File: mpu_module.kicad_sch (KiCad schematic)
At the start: 11 parts

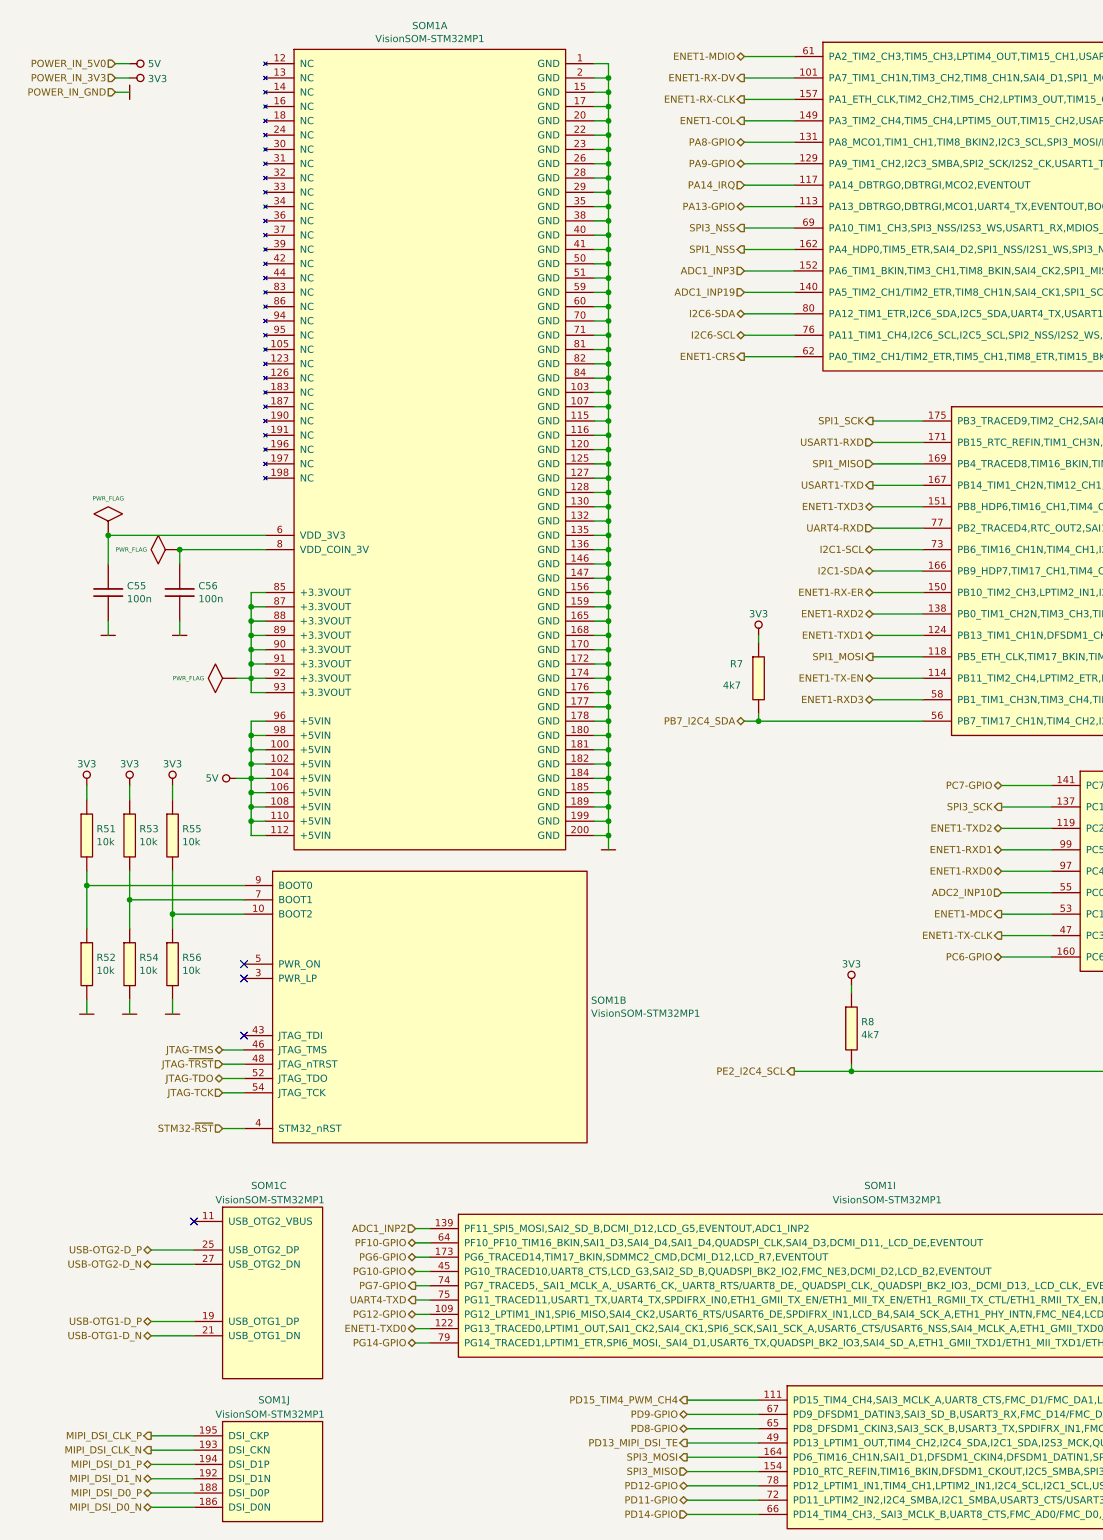
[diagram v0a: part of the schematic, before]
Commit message: Corrected schematic
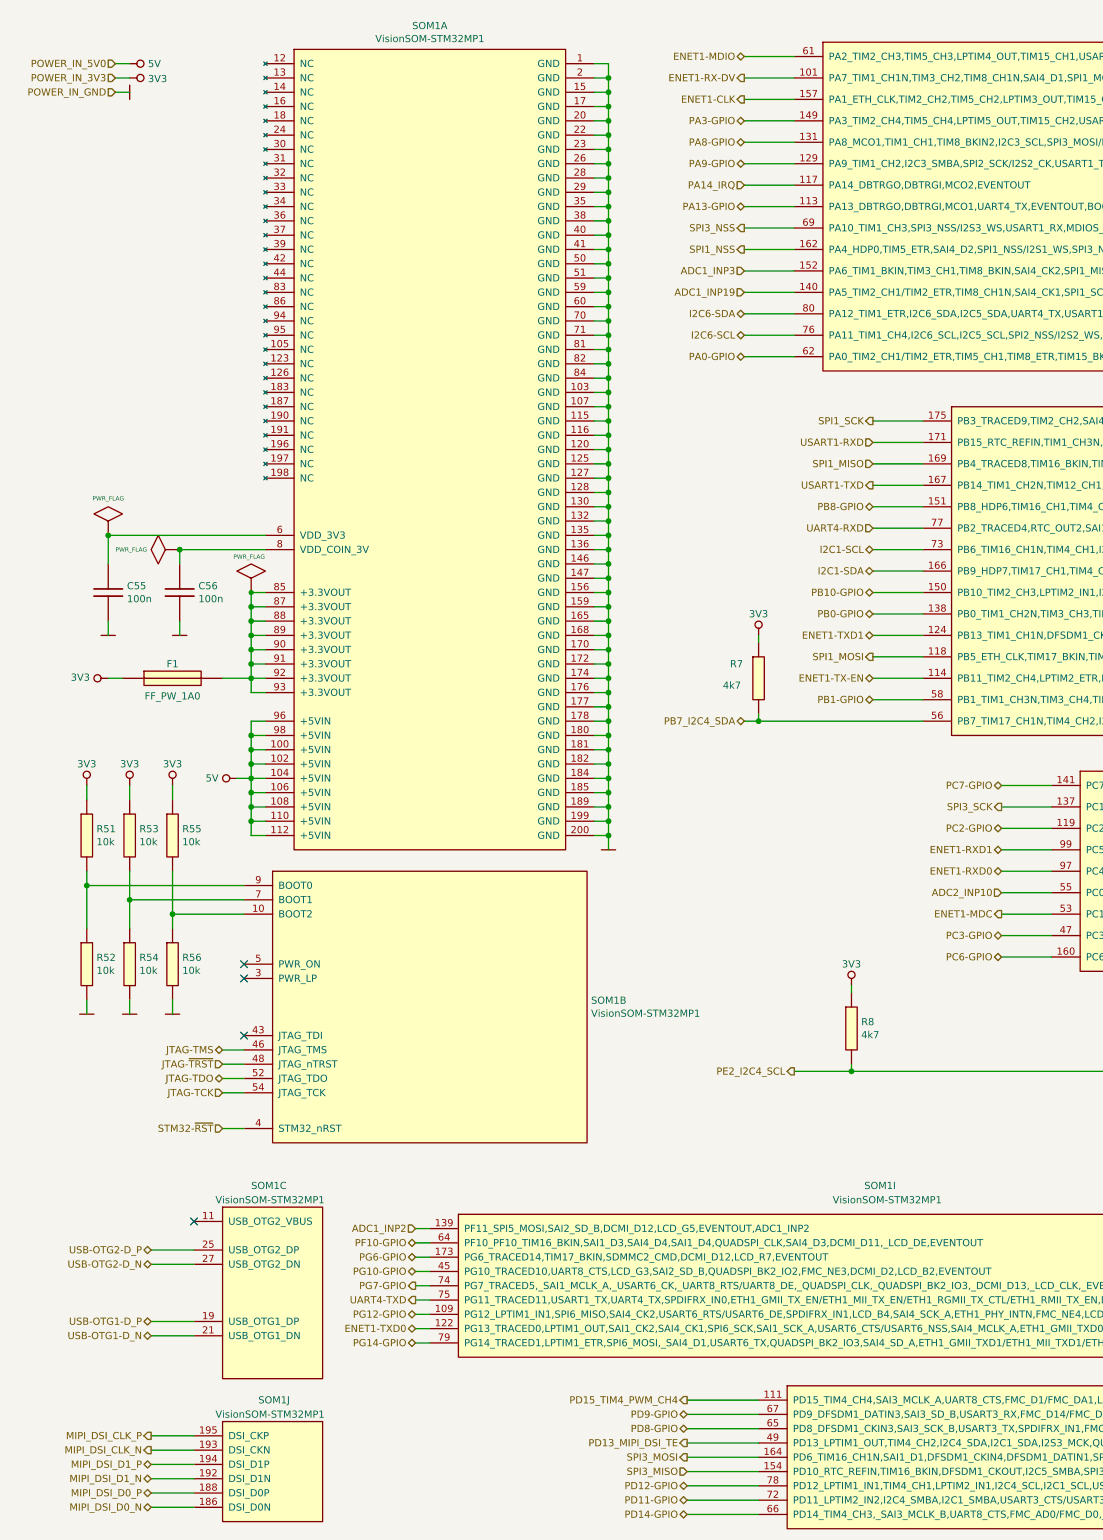
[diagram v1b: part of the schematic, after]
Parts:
- added F1: FF_PW_1A0, Smd_Fuses:Fuse_0603-FF_PW_1A0, symbol Smd_Fuses:FF_PW_1A0
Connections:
- net 3V3: now also F1.1
- net at SOM1.85 (+3.3VOUT), SOM1.87 (+3.3VOUT), SOM1.88 (+3.3VOUT)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: now also F1.2
- net ENET1-COL renamed PA3-GPIO
- net ENET1-CRS renamed PA0-GPIO
- net ENET1-RX-CLK renamed ENET1-CLK
- net ENET1-RX-ER renamed PB10-GPIO
- net ENET1-RXD2 renamed PB0-GPIO
- net ENET1-RXD3 renamed PB1-GPIO
- net ENET1-TX-CLK renamed PC3-GPIO
- net ENET1-TXD2 renamed PC2-GPIO
- net ENET1-TXD3 renamed PB8-GPIO
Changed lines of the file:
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@@
   (junction (at 118.11 158.75) (diameter 1.016) (color 0 0 0 0)
   )
+  (junction (at 54.61 115.57) (diameter 0) (color 0 0 0 0)
+  )
   (junction (at 118.11 135.89) (diameter 1.016) (color 0 0 0 0)
   )
@@
     (stroke (width 0) (type solid) (color 0 0 0 0))
   )
-  (wire (pts (xy 54.61 130.81) (xy 52.07 130.81))
-    (stroke (width 0) (type solid) (color 0 0 0 0))
-  )
   (wire (pts (xy 118.11 80.01) (xy 118.11 82.55))
     (stroke (width 0) (type solid) (color 0 0 0 0))
@@
     (stroke (width 0) (type solid) (color 0 0 0 0))
   )
+  (wire (pts (xy 29.21 130.81) (xy 31.75 130.81))
+    (stroke (width 0) (type default) (color 0 0 0 0))
+  )
   (wire (pts (xy 86.36 248.92) (xy 83.82 248.92))
     (stroke (width 0) (type solid) (color 0 0 0 0))
@@
     (stroke (width 0) (type solid) (color 0 0 0 0))
   )
+  (wire (pts (xy 49.53 130.81) (xy 54.61 130.81))
+    (stroke (width 0) (type default) (color 0 0 0 0))
+  )
   (wire (pts (xy 173.99 111.76) (xy 165.1 111.76))
     (stroke (width 0) (type solid) (color 0 0 0 0))
@@
     )
   )
-  (hierarchical_label "ENET1-COL" (shape output) (at 142.24 31.75 180)
-    (effects (font (size 1.27 1.27)) (justify right))
-  )
   (hierarchical_label "SPI3_MOSI" (shape output) (at 132.08 269.24 180)
     (effects (font (size 1.27 1.27)) (justify right))
@@
     (effects (font (size 1.27 1.27)) (justify right))
   )
-  (hierarchical_label "ENET1-TXD2" (shape bidirectional) (at 187.96 157.48 180)
-    (effects (font (size 1.27 1.27)) (justify right))
-  )
   (hierarchical_label "PG6-GPIO" (shape bidirectional) (at 83.82 233.68 180)
     (effects (font (size 1.27 1.27)) (justify right))
@@
     (effects (font (size 1.27 1.27)) (justify right))
   )
+  (hierarchical_label "PC3-GPIO" (shape bidirectional) (at 187.96 176.53 180)
+    (effects (font (size 1.27 1.27)) (justify right))
+  )
   (hierarchical_label "UART4-TXD" (shape output) (at 83.82 241.3 180)
     (effects (font (size 1.27 1.27)) (justify right))
   )
-  (hierarchical_label "USB-OTG1-D_P" (shape bidirectional) (at 36.83 245.11 180)
+  (hierarchical_label "PA3-GPIO" (shape bidirectional) (at 142.24 31.75 180)
     (effects (font (size 1.27 1.27)) (justify right))
   )
-  (hierarchical_label "SPI3_MISO" (shape input) (at 132.08 271.78 180)
+  (hierarchical_label "USB-OTG1-D_P" (shape bidirectional) (at 36.83 245.11 180)
     (effects (font (size 1.27 1.27)) (justify right))
   )
-  (hierarchical_label "ENET1-RXD2" (shape bidirectional) (at 165.1 119.38 180)
+  (hierarchical_label "SPI3_MISO" (shape input) (at 132.08 271.78 180)
     (effects (font (size 1.27 1.27)) (justify right))
   )
@@
     (effects (font (size 1.27 1.27)) (justify right))
   )
-  (hierarchical_label "ENET1-RXD3" (shape bidirectional) (at 165.1 134.62 180)
+  (hierarchical_label "PA0-GPIO" (shape bidirectional) (at 142.24 73.66 180)
+    (effects (font (size 1.27 1.27)) (justify right))
+  )
+  (hierarchical_label "PB0-GPIO" (shape bidirectional) (at 165.1 119.38 180)
     (effects (font (size 1.27 1.27)) (justify right))
   )
@@
     (effects (font (size 1.27 1.27)) (justify right))
   )
-  (hierarchical_label "ENET1-CRS" (shape output) (at 142.24 73.66 180)
-    (effects (font (size 1.27 1.27)) (justify right))
-  )
   (hierarchical_label "ENET1-TXD1" (shape bidirectional) (at 165.1 123.19 180)
     (effects (font (size 1.27 1.27)) (justify right))
@@
     (effects (font (size 1.27 1.27)) (justify right))
   )
+  (hierarchical_label "PC2-GPIO" (shape bidirectional) (at 187.96 157.48 180)
+    (effects (font (size 1.27 1.27)) (justify right))
+  )
   (hierarchical_label "PD8-GPIO" (shape bidirectional) (at 132.08 264.16 180)
     (effects (font (size 1.27 1.27)) (justify right))
@@
     (effects (font (size 1.27 1.27)) (justify right))
   )
-  (hierarchical_label "ENET1-TXD3" (shape bidirectional) (at 165.1 100.33 180)
-    (effects (font (size 1.27 1.27)) (justify right))
-  )
-  (hierarchical_label "ENET1-TX-CLK" (shape output) (at 187.96 176.53 180)
+  (hierarchical_label "PB1-GPIO" (shape bidirectional) (at 165.1 134.62 180)
     (effects (font (size 1.27 1.27)) (justify right))
   )
@@
     (effects (font (size 1.27 1.27)) (justify right))
   )
-  (hierarchical_label "ENET1-RX-ER" (shape bidirectional) (at 165.1 115.57 180)
+  (hierarchical_label "PB8-GPIO" (shape bidirectional) (at 165.1 100.33 180)
     (effects (font (size 1.27 1.27)) (justify right))
   )
-  (hierarchical_label "ENET1-RX-CLK" (shape output) (at 142.24 27.94 180)
+  (hierarchical_label "ENET1-CLK" (shape output) (at 142.24 27.94 180)
     (effects (font (size 1.27 1.27)) (justify right))
   )
@@
     (effects (font (size 1.27 1.27)) (justify right))
   )
-  (hierarchical_label "PD14-GPIO" (shape input) (at 132.08 279.4 180)
+  (hierarchical_label "PD14-GPIO" (shape bidirectional) (at 132.08 279.4 180)
     (effects (font (size 1.27 1.27)) (justify right))
   )
@@
     (effects (font (size 1.27 1.27)) (justify right))
   )
+  (hierarchical_label "PB10-GPIO" (shape bidirectional) (at 165.1 115.57 180)
+    (effects (font (size 1.27 1.27)) (justify right))
+  )
   (hierarchical_label "PB7_I2C4_SDA" (shape bidirectional) (at 142.24 138.43 180)
     (effects (font (size 1.27 1.27)) (justify right))
@@
     (pin "1")
   )
-  (symbol (lib_id "power:PWR_FLAG") (at 52.07 130.81 90) (unit 1)
+  (symbol (lib_id "power:PWR_FLAG") (at 54.61 115.57 0) (unit 1)
     (in_bom yes) (on_board yes)
-    (property "Reference" "#FLG0107" (id 0) (at 45.212 130.81 0)
+    (property "Reference" "#FLG0107" (id 0) (at 54.61 108.712 0)
       (effects (font (size 0.762 0.762)) hide)
     )
-    (property "Value" "PWR_FLAG" (id 1) (at 46.2788 130.81 90)
+    (property "Value" "PWR_FLAG" (id 1) (at 51.435 109.22 0)
       (effects (font (size 0.762 0.762)) (justify left))
     )
-    (property "Footprint" "" (id 2) (at 52.07 130.81 0)
+    (property "Footprint" "" (id 2) (at 54.61 115.57 0)
       (effects (font (size 1.524 1.524)))
     )
-    (property "Datasheet" "" (id 3) (at 52.07 130.81 0)
+    (property "Datasheet" "" (id 3) (at 54.61 115.57 0)
       (effects (font (size 1.524 1.524)))
     )
@@
     (pin "1")
   )
+  (symbol (lib_id "power:3V3_NO_GLOBAL") (at 29.21 130.81 90) (unit 1)
+    (in_bom yes) (on_board yes)
+    (property "Reference" "#PWR76" (id 0) (at 26.67 130.81 0)
+      (effects (font (size 1.016 1.016)) hide)
+    )
+    (property "Value" "3V3" (id 1) (at 25.9588 130.6576 90)
+      (effects (font (size 1.27 1.27)) (justify left))
+    )
+    (property "Footprint" "" (id 2) (at 29.21 130.81 0)
+      (effects (font (size 1.524 1.524)))
+    )
+    (property "Datasheet" "" (id 3) (at 29.21 130.81 0)
+      (effects (font (size 1.524 1.524)))
+    )
+    (pin "1")
+  )
+  (symbol (lib_id "Smd_Fuses:FF_PW_1A0") (at 40.64 130.81 0) (unit 1)
+    (in_bom yes) (on_board yes)
+    (property "Reference" "F1" (id 0) (at 40.64 128.27 0))
+    (property "Value" "FF_PW_1A0" (id 1) (at 40.64 133.985 0))
+    (property "Footprint" "Smd_Fuses:Fuse_0603-FF_PW_1A0" (id 2) (at 40.64 142.24 0)
+      (effects (font (size 1.27 1.27)) hide)
+    )
+    (property "Datasheet" "https://www.tme.eu/Document/d23fed0116a9e0192c3db408cb2a3cd4/81.pdf" (id 3) (at 40.64 142.24 0)
+      (effects (font (size 1.27 1.27)) hide)
+    )
+    (property "Manufacturer" "ESKA" (id 4) (at 40.64 130.81 0)
+      (effects (font (size 1.27 1.27)) hide)
+    )
+    (property "Manufacturer Part Number" "FUSE 0603-FF PW 1A" (id 5) (at 40.64 130.81 0)
+      (effects (font (size 1.27 1.27)) hide)
+    )
+    (property "Supplier" "Tme" (id 6) (at 40.64 130.81 0)
+      (effects (font (size 1.27 1.27)) hide)
+    )
+    (property "Supplier Part Number" "BSMD0603-SS1.0" (id 7) (at 40.64 130.81 0)
+      (effects (font (size 1.27 1.27)) hide)
+    )
+    (property "URL" "https://www.tme.eu/pl/details/bsmd0603-ss1.0/bezpieczniki-smd-0603-superszybkie/eska/fuse-0603-ff-pw-1a0/" (id 8) (at 40.64 130.81 0)
+      (effects (font (size 1.27 1.27)) hide)
+    )
+    (property "Price@1pc" "0,95" (id 9) (at 40.64 130.81 0)
+      (effects (font (size 1.27 1.27)) hide)
+    )
+    (property "Price@1000pcs" "0,55" (id 10) (at 40.64 130.81 0)
+      (effects (font (size 1.27 1.27)) hide)
+    )
+    (property "Developer" "MW" (id 11) (at 40.64 130.81 0)
+      (effects (font (size 1.27 1.27)) hide)
+    )
+    (property "Package" "0603" (id 12) (at 40.64 130.81 0)
+      (effects (font (size 1.27 1.27)) hide)
+    )
+    (property "LCSC Part #(optional)" "" (id 13) (at 40.64 130.81 0)
+      (effects (font (size 1.27 1.27)) hide)
+    )
+    (pin "1")
+    (pin "2")
+  )
 )

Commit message: Rebuild board
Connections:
- net ENET1-RX-DV renamed ENET1-CRS-DV
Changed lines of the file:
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@@
     (effects (font (size 1.27 1.27)) (justify right))
   )
-  (hierarchical_label "ENET1-RX-DV" (shape output) (at 142.24 24.13 180)
+  (hierarchical_label "ENET1-CRS-DV" (shape output) (at 142.24 24.13 180)
     (effects (font (size 1.27 1.27)) (justify right))
   )

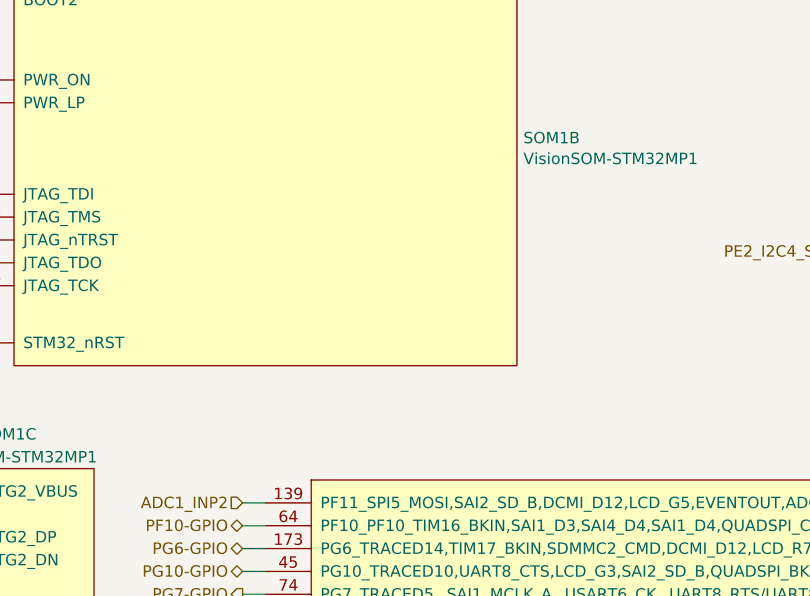
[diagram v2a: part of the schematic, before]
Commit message: Cleared all errors DRC
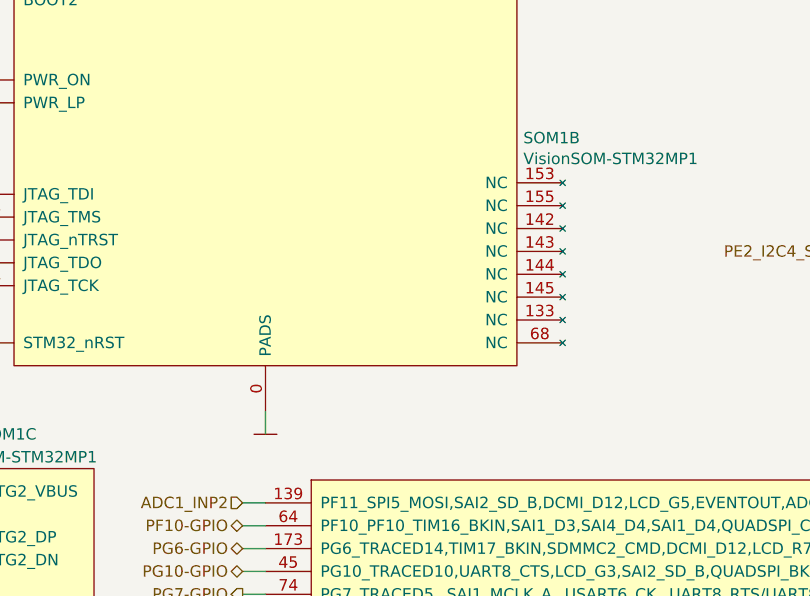
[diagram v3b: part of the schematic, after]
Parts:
- R51, R52, R53, R54, R55, R56: LCSC Part #(optional) (none) -> C269684
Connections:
- net GND: now also SOM1.0 (PADS)
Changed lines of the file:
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@@
+    (stroke (width 0) (type solid) (color 0 0 0 0))
+  )
+  (wire (pts (xy 86.36 218.44) (xy 86.36 220.98))
     (stroke (width 0) (type solid) (color 0 0 0 0))
   )
@@
       (effects (font (size 1.27 1.27)) hide)
     )
+    (pin "0")
     (pin "10")
+    (pin "133")
+    (pin "142")
+    (pin "143")
+    (pin "144")
+    (pin "145")
+    (pin "153")
+    (pin "155")
     (pin "3")
     (pin "4")
@@
     (pin "52")
     (pin "54")
+    (pin "68")
     (pin "7")
     (pin "9")
@@
       (effects (font (size 1.27 1.27)) hide)
     )
+    (property "LCSC Part #(optional)" "C269684" (id 13) (at 25.4 158.75 0)
+      (effects (font (size 1.27 1.27)) hide)
+    )
     (pin "1")
     (pin "2")
@@
       (effects (font (size 1.27 1.27)) hide)
     )
+    (property "LCSC Part #(optional)" "C269684" (id 13) (at 33.02 158.75 0)
+      (effects (font (size 1.27 1.27)) hide)
+    )
     (pin "1")
     (pin "2")
@@
       (effects (font (size 1.27 1.27)) hide)
     )
+    (property "LCSC Part #(optional)" "C269684" (id 13) (at 40.64 158.75 0)
+      (effects (font (size 1.27 1.27)) hide)
+    )
     (pin "1")
     (pin "2")
@@
       (effects (font (size 1.27 1.27)) hide)
     )
+    (property "LCSC Part #(optional)" "C269684" (id 13) (at 25.4 181.61 0)
+      (effects (font (size 1.27 1.27)) hide)
+    )
     (pin "1")
     (pin "2")
@@
       (effects (font (size 1.27 1.27)) hide)
     )
+    (property "LCSC Part #(optional)" "C269684" (id 13) (at 33.02 181.61 0)
+      (effects (font (size 1.27 1.27)) hide)
+    )
     (pin "1")
     (pin "2")
@@
       (effects (font (size 1.27 1.27)) hide)
     )
+    (property "LCSC Part #(optional)" "C269684" (id 13) (at 40.64 181.61 0)
+      (effects (font (size 1.27 1.27)) hide)
+    )
     (pin "1")
     (pin "2")
@@
       (effects (font (size 1.524 1.524)))
     )
+    (pin "1")
+  )
+  (symbol (lib_id "power:GND") (at 86.36 220.98 0) (unit 1)
+    (in_bom yes) (on_board yes)
+    (property "Reference" "#PWR0233" (id 0) (at 86.36 218.44 0)
+      (effects (font (size 0.762 0.762)) hide)
+    )
+    (property "Value" "GND" (id 1) (at 86.36 223.52 0)
+      (effects (font (size 0.762 0.762)) hide)
+    )
+    (property "Footprint" "" (id 2) (at 86.36 220.98 0)
+      (effects (font (size 1.524 1.524)))
+    )
+    (property "Datasheet" "" (id 3) (at 86.36 220.98 0)
+      (effects (font (size 1.524 1.524)))
+    )
